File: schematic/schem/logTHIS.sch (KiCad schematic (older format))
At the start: 16 parts, among them K1 Sensor1, K2 Sensor0, P1 CONN_6, P2 Battery, P3 I2C Sense, Q1 MOSFET_N, U1 24AA1025, U2 DS1337, U3 ATTINY85V, X1 32.768 kHz

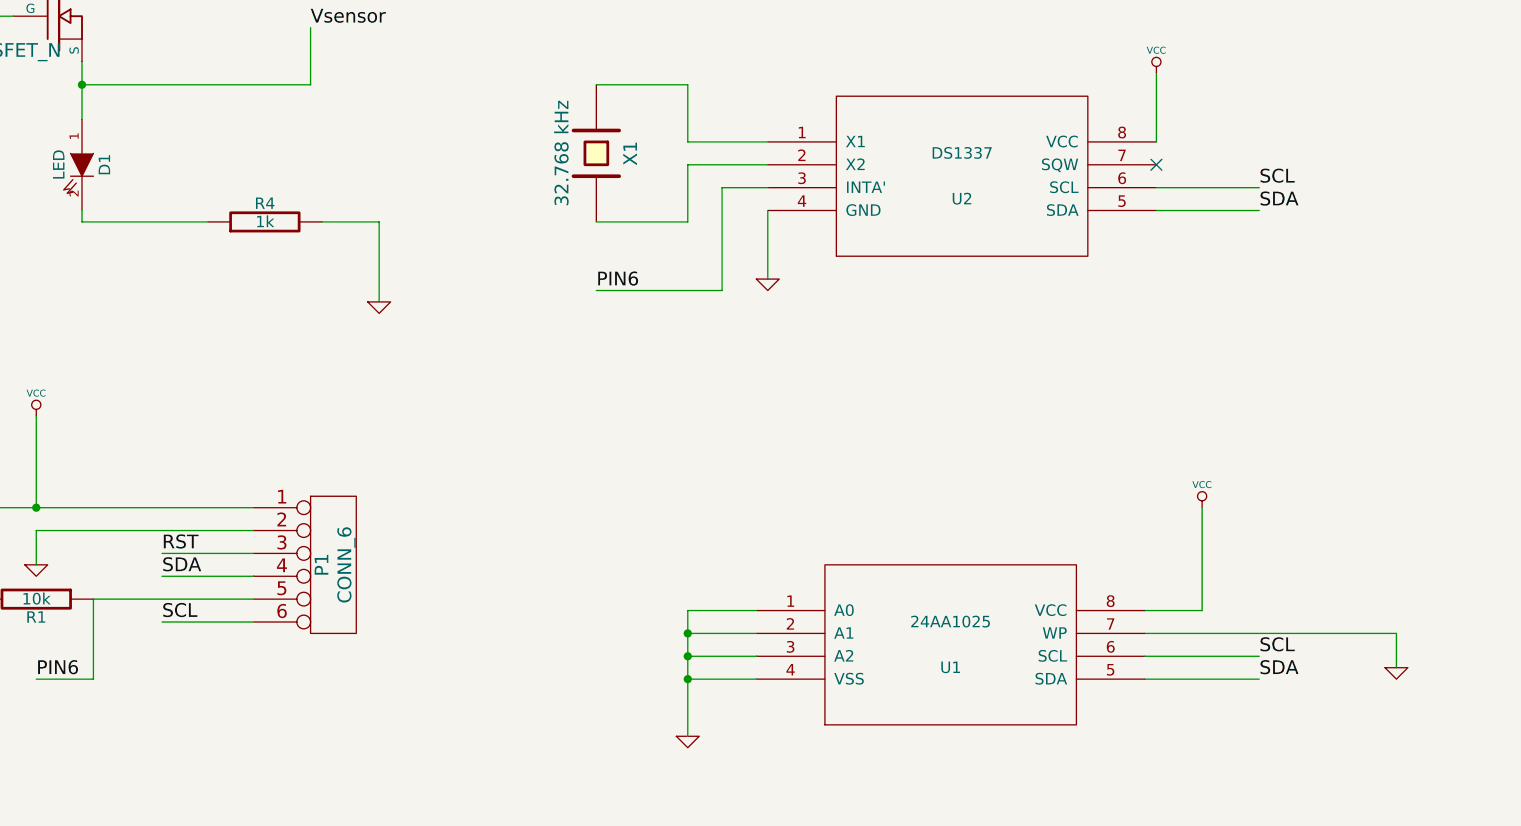
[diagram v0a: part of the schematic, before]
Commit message: had I2C bus seperated.  Connected it, relaid the PCB, regernated the gerber and drill files.
I had two I2C buses, one that was (SCK, SDA) and the other being (I2C_CLK, I2C_DAT).  Merged
the two into (I2C_CLK, I2C_DAT) and (just barely) managed to lay out the PCB into a single
layer.
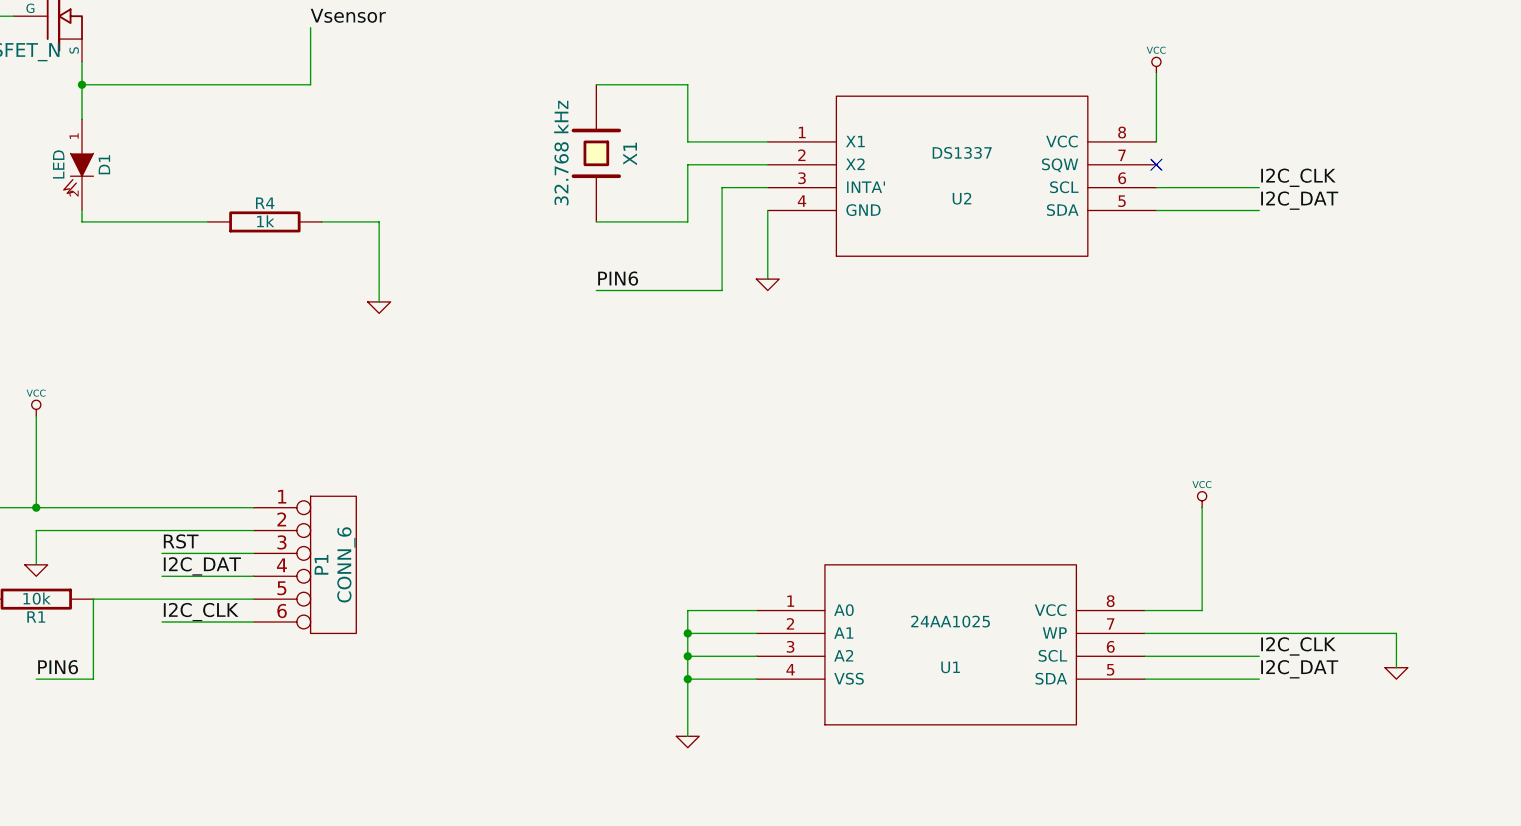
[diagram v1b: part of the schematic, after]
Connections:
- net labels removed: SCL, SDA
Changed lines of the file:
@@
-EESchema Schematic File Version 2  date Mon 24 Dec 2012 04:09:19 AM EST
+EESchema Schematic File Version 2  date Wed 26 Dec 2012 11:09:31 PM EST
 LIBS:power
 LIBS:device
@@
 Sheet 1 1
 Title "logTHIS main board"
-Date "20 dec 2012"
+Date "27 dec 2012"
 Rev "1"
 Comp ""
@@
 Comment4 ""
 $EndDescr
+Text Label 6600 5550 0    60   ~ 0
+I2C_DAT
+Text Label 6600 3500 0    60   ~ 0
+I2C_DAT
+Text Label 6600 5450 0    60   ~ 0
+I2C_CLK
+Text Label 6600 3400 0    60   ~ 0
+I2C_CLK
+Text Label 1800 5300 0    60   ~ 0
+I2C_CLK
+Text Label 1800 5100 0    60   ~ 0
+I2C_DAT
 Connection ~ 8800 2350
 Wire Wire Line
@@
 	0    1    1    0
 $EndComp
-Text Label 1800 5300 0    60   ~ 0
-SCL
-Text Label 1800 5100 0    60   ~ 0
-SDA
 Text Label 1800 5000 0    60   ~ 0
 RST
@@
 	1    0    0    -1
 $EndComp
-Text Label 6600 5550 0    60   ~ 0
-SDA
-Text Label 6600 5450 0    60   ~ 0
-SCL
 $Comp
 L VCC #PWR03
@@
 	1    0    0    -1
 $EndComp
-Text Label 6600 3500 0    60   ~ 0
-SDA
-Text Label 6600 3400 0    60   ~ 0
-SCL
 Text Label 6700 1900 0    60   ~ 0
 I2C_DAT

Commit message: bug fix: 1M EEPROM needs A2 tied hi
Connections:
- wire segments 90 -> 91

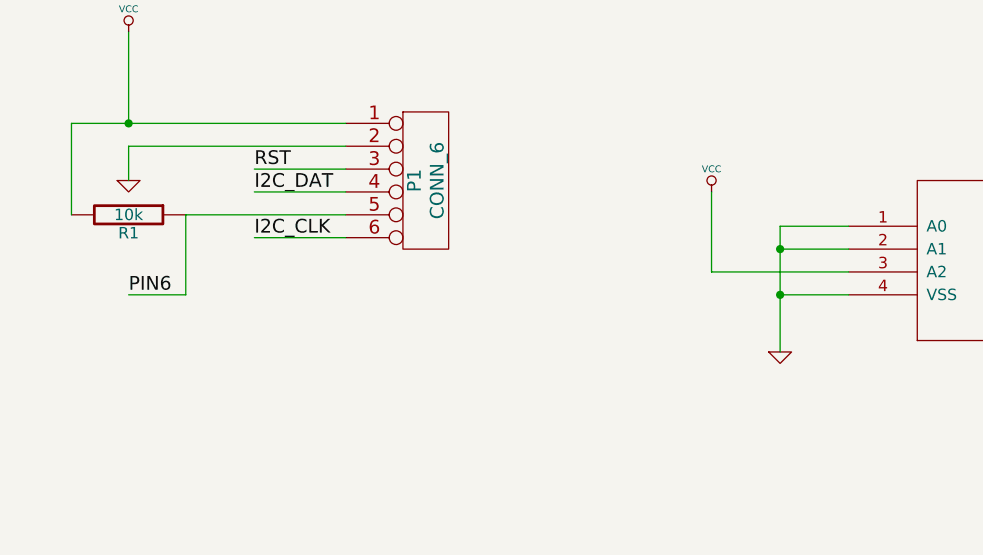
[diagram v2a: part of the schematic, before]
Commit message: added power jumper to ease single board layout
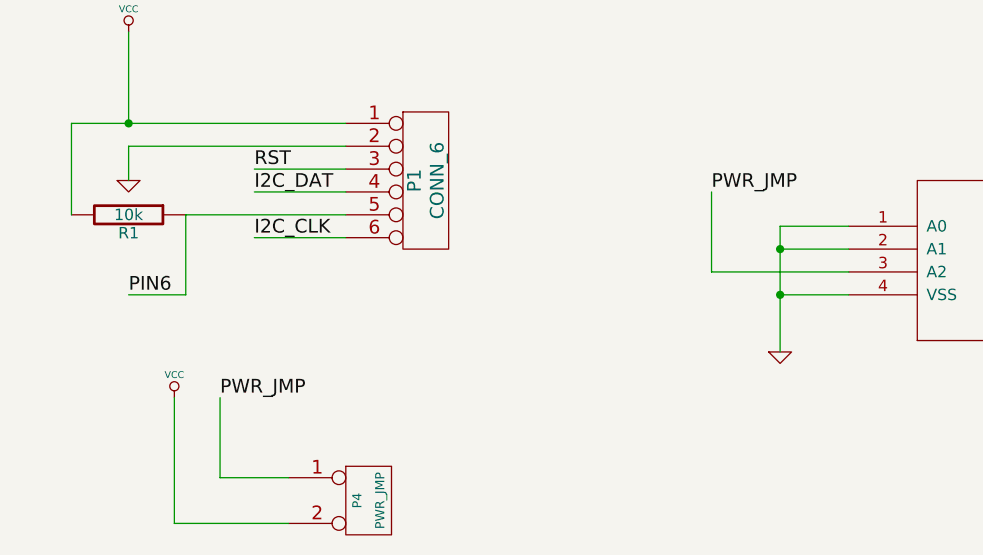
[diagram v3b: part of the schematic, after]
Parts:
- added P4: PWR_JMP, symbol CONN_2
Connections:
- net labels added: PWR_JMP
- wire segments 91 -> 95
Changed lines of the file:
@@
-EESchema Schematic File Version 2  date Wed 02 Jan 2013 11:50:17 PM EST
+EESchema Schematic File Version 2  date Thu 03 Jan 2013 12:28:26 AM EST
 LIBS:power
 LIBS:device
@@
 Comment4 ""
 $EndDescr
+Text Label 1650 6000 0    60   ~ 0
+PWR_JMP
+Wire Wire Line
+	1650 6000 1650 6350
+Wire Wire Line
+	1650 6350 1950 6350
+Wire Wire Line
+	3800 5100 3800 5450
+Wire Wire Line
+	3800 5450 4400 5450
+Connection ~ 9450 1750
+Wire Wire Line
+	9450 1750 9050 1750
+Wire Wire Line
+	3700 3850 4250 3850
+Wire Wire Line
+	4250 3850 4250 3400
+Connection ~ 1250 4800
+Wire Wire Line
+	2200 4800 1000 4800
+Wire Wire Line
+	1000 4800 1000 5200
+Wire Wire Line
+	1800 5300 2200 5300
+Wire Wire Line
+	1800 5100 2200 5100
+Wire Wire Line
+	2200 4900 1250 4900
+Wire Wire Line
+	1250 4900 1250 5050
+Wire Wire Line
+	6100 5550 6600 5550
+Wire Wire Line
+	7200 5500 7200 5350
+Wire Wire Line
+	7200 5350 6100 5350
+Wire Wire Line
+	6150 3400 6600 3400
+Wire Wire Line
+	7150 1250 7150 1100
+Wire Wire Line
+	7150 1100 6950 1100
+Wire Wire Line
+	6150 1800 6700 1800
+Wire Wire Line
+	4450 1800 3850 1800
+Wire Wire Line
+	4450 1600 3850 1600
+Wire Wire Line
+	8150 2350 9600 2350
+Wire Wire Line
+	9600 2350 9600 2100
+Wire Wire Line
+	9600 2100 9850 2100
+Wire Wire Line
+	9450 1550 9450 1900
+Wire Wire Line
+	9450 1900 9850 1900
+Wire Wire Line
+	9900 3650 9300 3650
+Wire Wire Line
+	9300 3650 9300 3750
+Wire Wire Line
+	8950 6100 9500 6100
+Wire Wire Line
+	9500 6100 9500 5700
+Wire Wire Line
+	9500 5700 9700 5700
+Wire Wire Line
+	9250 5250 9250 5500
+Wire Wire Line
+	9250 5500 9700 5500
+Connection ~ 2125 1075
+Wire Wire Line
+	2125 925  2125 1075
+Wire Wire Line
+	1925 825  1925 1075
+Wire Wire Line
+	1925 1075 2325 1075
+Wire Wire Line
+	1450 2450 1450 1950
+Wire Wire Line
+	2000 3550 1450 3550
+Wire Wire Line
+	1450 3550 1450 3500
+Wire Wire Line
+	6350 4800 6350 5250
+Wire Wire Line
+	6350 5250 6100 5250
+Connection ~ 4100 5550
+Wire Wire Line
+	4100 5550 4400 5550
+Connection ~ 4100 5350
+Wire Wire Line
+	4400 5350 4100 5350
+Wire Wire Line
+	4450 1900 4450 2250
+Wire Wire Line
+	6150 3200 6150 2900
+Wire Wire Line
+	3700 2950 4100 2950
+Wire Wire Line
+	4100 2950 4100 3200
+Wire Wire Line
+	4100 3200 4450 3200
+Wire Wire Line
+	4450 3500 4450 3800
+Wire Wire Line
+	3700 3550 4100 3550
+Wire Wire Line
+	4100 3550 4100 3300
+Wire Wire Line
+	4100 3300 4450 3300
+Wire Wire Line
+	6150 1600 6150 750
+Wire Wire Line
+	4400 5250 4100 5250
+Wire Wire Line
+	4100 5250 4100 5800
+Wire Wire Line
+	4250 3400 4450 3400
+Wire Wire Line
+	1450 3100 1450 2850
+Wire Wire Line
+	2500 3550 2750 3550
+Wire Wire Line
+	2750 3550 2750 3900
+Wire Wire Line
+	1925 1525 1925 1275
+Wire Wire Line
+	1925 1275 2325 1275
+Wire Wire Line
+	2175 1425 2175 1275
+Connection ~ 2175 1275
+Wire Wire Line
+	1450 2950 2450 2950
+Connection ~ 1450 2950
+Wire Wire Line
+	2450 2950 2450 2700
+Wire Wire Line
+	9250 5750 9250 5600
+Wire Wire Line
+	9250 5600 9700 5600
+Wire Wire Line
+	9900 3550 9300 3550
+Wire Wire Line
+	9300 3550 9300 3400
+Wire Wire Line
+	9900 3750 9500 3750
+Wire Wire Line
+	9500 3750 9500 4100
+Wire Wire Line
+	9500 4100 8950 4100
+Wire Wire Line
+	9450 2100 9450 2000
+Wire Wire Line
+	9450 2000 9850 2000
+Wire Wire Line
+	9850 2200 9750 2200
+Wire Wire Line
+	9750 2200 9750 2650
+Wire Wire Line
+	9750 2650 8150 2650
+Wire Wire Line
+	4450 1700 3850 1700
+Wire Wire Line
+	6150 1700 6700 1700
+Wire Wire Line
+	6150 1900 6700 1900
+Wire Wire Line
+	6550 1100 6150 1100
+Connection ~ 6150 1100
+Wire Wire Line
+	6150 3500 6600 3500
+Wire Wire Line
+	6100 5450 6600 5450
+Wire Wire Line
+	1250 4400 1250 4800
+Wire Wire Line
+	2200 5000 1800 5000
+Wire Wire Line
+	2200 5200 1500 5200
+Wire Wire Line
+	1500 5200 1500 5550
+Wire Wire Line
+	1500 5550 1250 5550
+Wire Wire Line
+	1150 2650 750  2650
+Wire Wire Line
+	8800 1750 8800 1600
+Wire Wire Line
+	8800 1600 9450 1600
+Connection ~ 9450 1600
+Wire Wire Line
+	9050 2250 9050 2650
+Connection ~ 9050 2650
+Wire Wire Line
+	8800 2250 8800 2350
+Connection ~ 8800 2350
+Wire Wire Line
+	1950 6550 1450 6550
+Wire Wire Line
+	1450 6550 1450 6000
+Text Label 3800 5100 0    60   ~ 0
+PWR_JMP
 $Comp
 L VCC #PWR01
-U 1 1 50E4FC11
-P 3800 5100
-F 0 "#PWR01" H 3800 5200 30  0001 C CNN
-F 1 "VCC" H 3800 5200 30  0000 C CNN
-	1    3800 5100
+U 1 1 50E515BE
+P 1450 6000
+F 0 "#PWR01" H 1450 6100 30  0001 C CNN
+F 1 "VCC" H 1450 6100 30  0000 C CNN
+	1    1450 6000
 	1    0    0    -1
 $EndComp
-Wire Wire Line
-	3800 5100 3800 5450
-Wire Wire Line
-	3800 5450 4400 5450
-Connection ~ 9450 1750
-Wire Wire Line
-	9450 1750 9050 1750
-Wire Wire Line
-	3700 3850 4250 3850
-Wire Wire Line
-	4250 3850 4250 3400
-Connection ~ 1250 4800
-Wire Wire Line
-	2200 4800 1000 4800
-Wire Wire Line
-	1000 4800 1000 5200
-Wire Wire Line
-	1800 5300 2200 5300
-Wire Wire Line
-	1800 5100 2200 5100
-Wire Wire Line
-	2200 4900 1250 4900
-Wire Wire Line
-	1250 4900 1250 5050
-Wire Wire Line
-	6100 5550 6600 5550
-Wire Wire Line
-	7200 5500 7200 5350
-Wire Wire Line
-	7200 5350 6100 5350
-Wire Wire Line
-	6150 3400 6600 3400
-Wire Wire Line
-	7150 1250 7150 1100
-Wire Wire Line
-	7150 1100 6950 1100
-Wire Wire Line
-	6150 1800 6700 1800
-Wire Wire Line
-	4450 1800 3850 1800
-Wire Wire Line
-	4450 1600 3850 1600
-Wire Wire Line
-	8150 2350 9600 2350
-Wire Wire Line
-	9600 2350 9600 2100
-Wire Wire Line
-	9600 2100 9850 2100
-Wire Wire Line
-	9450 1550 9450 1900
-Wire Wire Line
-	9450 1900 9850 1900
-Wire Wire Line
-	9900 3650 9300 3650
-Wire Wire Line
-	9300 3650 9300 3750
-Wire Wire Line
-	8950 6100 9500 6100
-Wire Wire Line
-	9500 6100 9500 5700
-Wire Wire Line
-	9500 5700 9700 5700
-Wire Wire Line
-	9250 5250 9250 5500
-Wire Wire Line
-	9250 5500 9700 5500
-Connection ~ 2125 1075
-Wire Wire Line
-	2125 925  2125 1075
-Wire Wire Line
-	1925 825  1925 1075
-Wire Wire Line
-	1925 1075 2325 1075
-Wire Wire Line
-	1450 2450 1450 1950
-Wire Wire Line
-	2000 3550 1450 3550
-Wire Wire Line
-	1450 3550 1450 3500
-Wire Wire Line
-	6350 4800 6350 5250
-Wire Wire Line
-	6350 5250 6100 5250
-Connection ~ 4100 5550
-Wire Wire Line
-	4100 5550 4400 5550
-Connection ~ 4100 5350
-Wire Wire Line
-	4400 5350 4100 5350
-Wire Wire Line
-	4450 1900 4450 2250
-Wire Wire Line
-	6150 3200 6150 2900
-Wire Wire Line
-	3700 2950 4100 2950
-Wire Wire Line
-	4100 2950 4100 3200
-Wire Wire Line
-	4100 3200 4450 3200
-Wire Wire Line
-	4450 3500 4450 3800
-Wire Wire Line
-	3700 3550 4100 3550
-Wire Wire Line
-	4100 3550 4100 3300
-Wire Wire Line
-	4100 3300 4450 3300
-Wire Wire Line
-	6150 1600 6150 750
-Wire Wire Line
-	4400 5250 4100 5250
-Wire Wire Line
-	4100 5250 4100 5800
-Wire Wire Line
-	4250 3400 4450 3400
-Wire Wire Line
-	1450 3100 1450 2850
-Wire Wire Line
-	2500 3550 2750 3550
-Wire Wire Line
-	2750 3550 2750 3900
-Wire Wire Line
-	1925 1525 1925 1275
-Wire Wire Line
-	1925 1275 2325 1275
-Wire Wire Line
-	2175 1425 2175 1275
-Connection ~ 2175 1275
-Wire Wire Line
-	1450 2950 2450 2950
-Connection ~ 1450 2950
-Wire Wire Line
-	2450 2950 2450 2700
-Wire Wire Line
-	9250 5750 9250 5600
-Wire Wire Line
-	9250 5600 9700 5600
-Wire Wire Line
-	9900 3550 9300 3550
-Wire Wire Line
-	9300 3550 9300 3400
-Wire Wire Line
-	9900 3750 9500 3750
-Wire Wire Line
-	9500 3750 9500 4100
-Wire Wire Line
-	9500 4100 8950 4100
-Wire Wire Line
-	9450 2100 9450 2000
-Wire Wire Line
-	9450 2000 9850 2000
-Wire Wire Line
-	9850 2200 9750 2200
-Wire Wire Line
-	9750 2200 9750 2650
-Wire Wire Line
-	9750 2650 8150 2650
-Wire Wire Line
-	4450 1700 3850 1700
-Wire Wire Line
-	6150 1700 6700 1700
-Wire Wire Line
-	6150 1900 6700 1900
-Wire Wire Line
-	6550 1100 6150 1100
-Connection ~ 6150 1100
-Wire Wire Line
-	6150 3500 6600 3500
-Wire Wire Line
-	6100 5450 6600 5450
-Wire Wire Line
-	1250 4400 1250 4800
-Wire Wire Line
-	2200 5000 1800 5000
-Wire Wire Line
-	2200 5200 1500 5200
-Wire Wire Line
-	1500 5200 1500 5550
-Wire Wire Line
-	1500 5550 1250 5550
-Wire Wire Line
-	1150 2650 750  2650
-Wire Wire Line
-	8800 1750 8800 1600
-Wire Wire Line
-	8800 1600 9450 1600
-Connection ~ 9450 1600
-Wire Wire Line
-	9050 2250 9050 2650
-Connection ~ 9050 2650
-Wire Wire Line
-	8800 2250 8800 2350
-Connection ~ 8800 2350
+$Comp
+L CONN_2 P4
+U 1 1 50E515A4
+P 2300 6450
+F 0 "P4" V 2250 6450 40  0000 C CNN
+F 1 "PWR_JMP" V 2350 6450 40  0000 C CNN
+	1    2300 6450
+	1    0    0    -1
+$EndComp
 Text Label 6600 5550 0    60   ~ 0
 I2C_DAT
